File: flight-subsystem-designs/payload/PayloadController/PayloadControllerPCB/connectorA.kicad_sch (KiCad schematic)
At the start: 2 parts, among them J1 FX10A-168P-SV71, J2 FX10A-168P-SV71

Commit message: Update plcl schematics
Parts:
- added R1, R3: 2.2k, symbol Device:R
- added R2: 10k, symbol Device:R
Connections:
- net 3V_S is gone; now on net 3V3_S: J1.86, J2.10, J2.12, J2.26, J2.29, J2.38, J2.41, J2.50
- net GND: now also J1.108, J1.109, J1.96, J1.99
- net 3V3_S: now reaches J2.74
- net 3V3_S: now also J2.77, R1.1, R2.1, R3.2
- net I2C_SCL: now reaches J1.111
- net I2C_SCL: now also R1.2
- net at J1.112: now also R2.2
- net I2C_SDA: now reaches J1.113
- net I2C_SDA: now also R3.1
- no-connect marks 60 -> 72

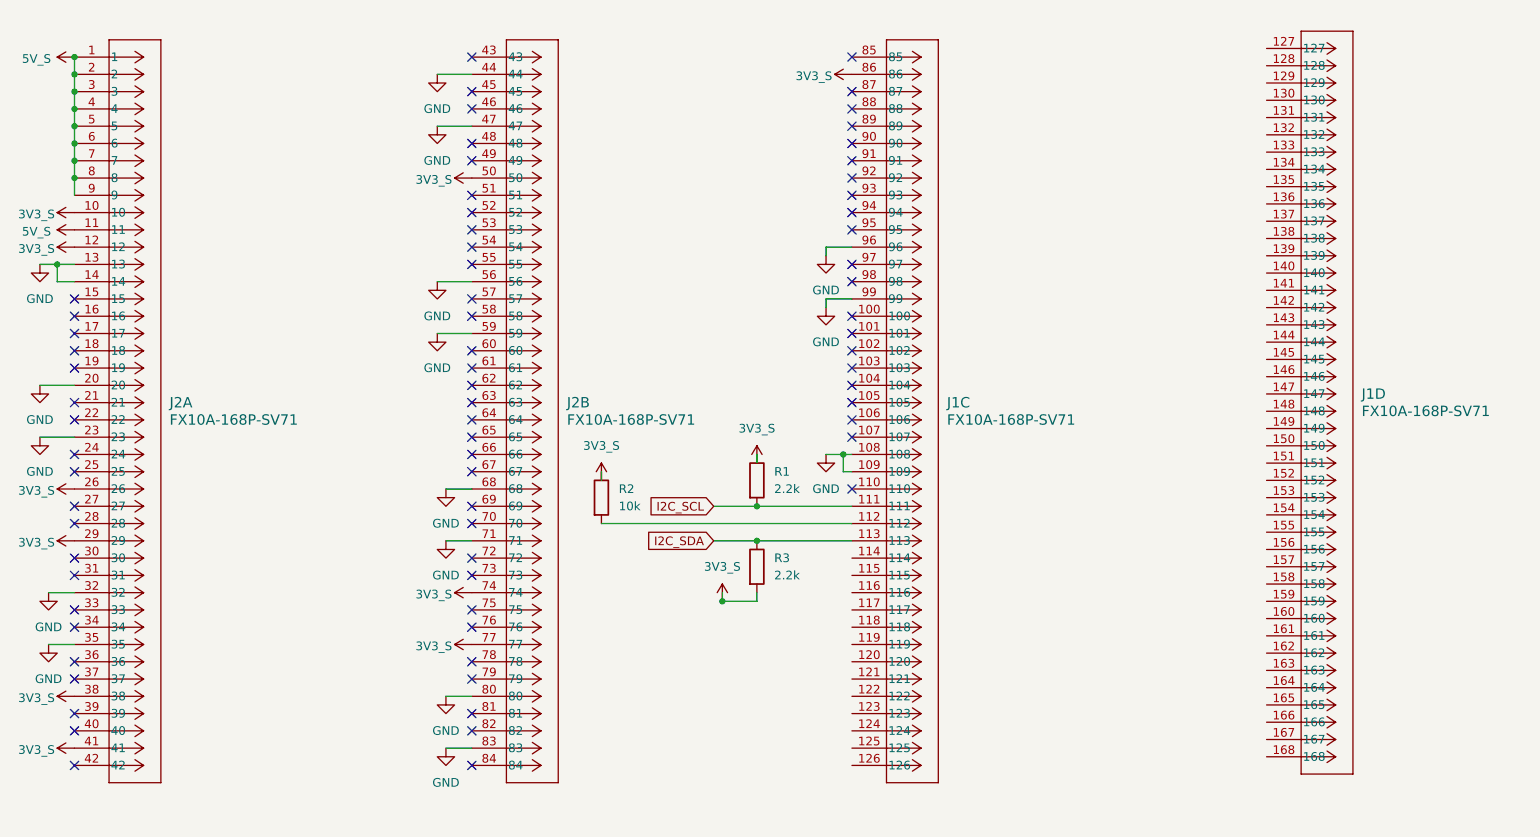
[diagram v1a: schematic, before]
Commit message: Update PC104 schematic
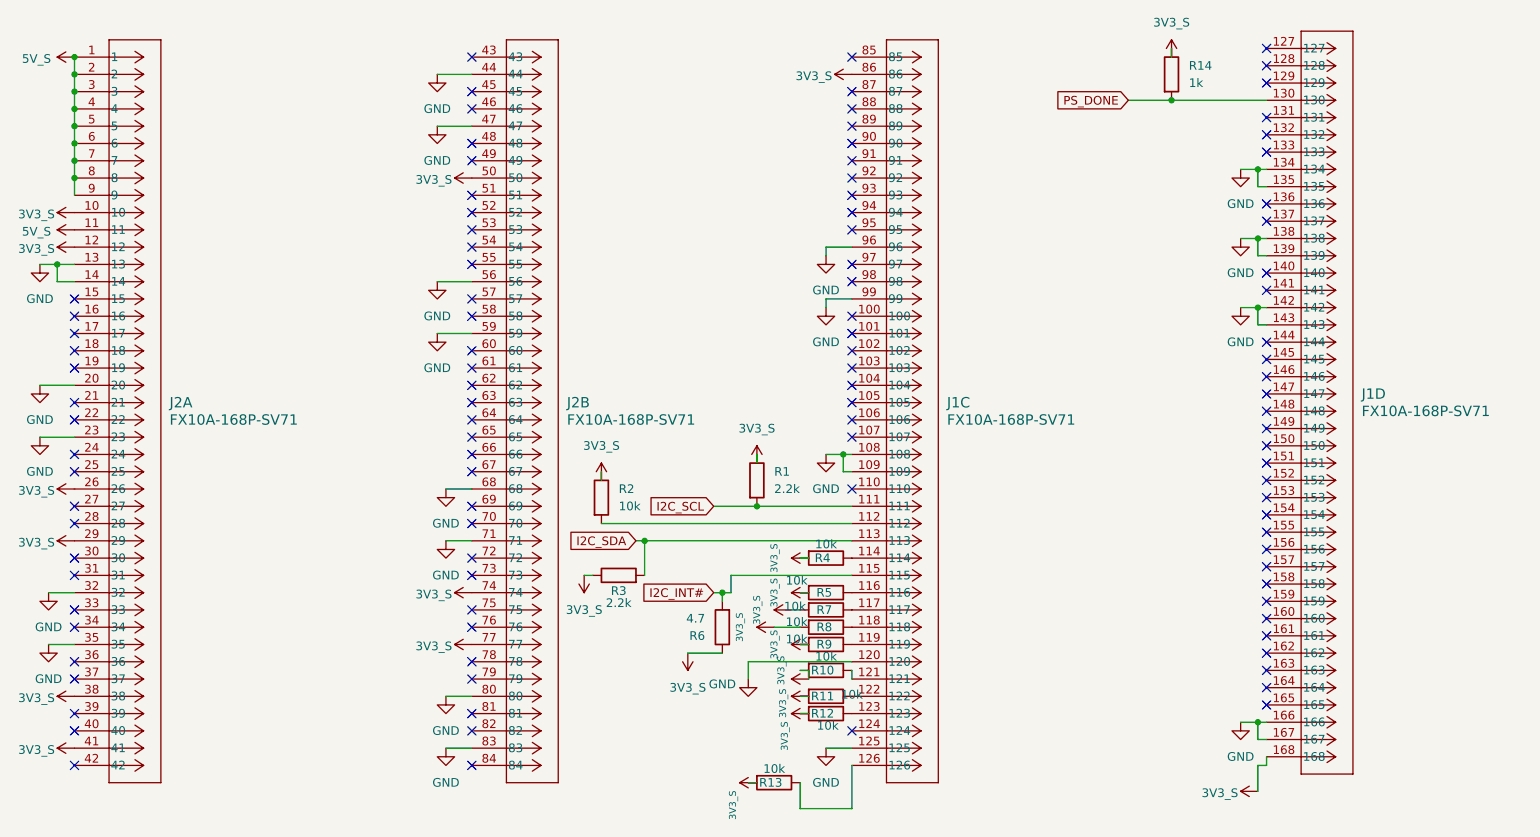
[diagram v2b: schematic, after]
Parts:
- added R10, R11, R12, R13, R4, R5, R7, R8, R9: 10k, symbol Device:R
- added R14: 1k, symbol Device:R
- added R6: 4.7, symbol Device:R
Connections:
- net 3V3_S: now also J1.168, R3.1, R10.2, R11.2, R12.2, R13.2, R14.1, R4.2, R5.2, R6.1, R7.2, R8.2, R9.2; no longer R3.2
- net GND: now also J1.120, J1.125, J1.134, J1.135, J1.138, J1.139, J1.142, J1.143, J1.166, J1.167
- net I2C_SDA: now also R3.2; no longer R3.1
- net PS_DONE: now reaches J1.130
- net PS_DONE: now also R14.2
- net at J1.114: now also R4.1
- net I2C_INT#: now reaches J1.115
- net I2C_INT#: now also R6.2
- net at J1.116: now also R5.1
- net at J1.117: now also R7.1
- net at J1.118: now also R8.1
- net at J1.119: now also R9.1
- net at J1.121: now also R10.1
- net at J1.122: now also R11.1
- net at J1.123: now also R12.1
- net at J1.126: now also R13.1
- no-connect marks 72 -> 105
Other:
- moved on the sheet: R3

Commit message: Update PLCL Schematic
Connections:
- net UARTRX1: now reaches J2.43
- net UARTTX1: now reaches J2.45
- net SHUTDOWN: now reaches J2.55
- net ALM: now reaches J2.79
- net UARTRX: now reaches J1.105
- net UARTTX: now reaches J1.107
- no-connect marks 105 -> 99
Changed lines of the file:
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@@
 	)
 	(no_connect
-		(at 165.1 95.25)
-	)
-	(no_connect
 		(at 165.1 64.77)
 	)
@@
 	)
 	(no_connect
-		(at 165.1 100.33)
-	)
-	(no_connect
 		(at 165.1 67.31)
 	)
@@
 	)
 	(no_connect
-		(at 109.22 135.89)
-	)
-	(no_connect
 		(at 50.8 102.87)
 	)
@@
 	)
 	(no_connect
-		(at 109.22 49.53)
-	)
-	(no_connect
 		(at 226.06 101.6)
 	)
@@
 	)
 	(no_connect
-		(at 109.22 74.93)
-	)
-	(no_connect
 		(at 109.22 133.35)
 	)
@@
 		(at 226.06 78.74)
 	)
-	(no_connect
-		(at 109.22 44.45)
-	)
 	(wire
 		(pts
@@
 	(wire
 		(pts
-			(xy 104.14 46.99) (xy 109.22 46.99)
+			(xy 96.52 46.99) (xy 109.22 46.99)
 		)
 		(stroke
@@
 		)
 	)
+	(global_label "ALM"
+		(shape input)
+		(at 109.22 135.89 180)
+		(fields_autoplaced yes)
+		(effects
+			(font
+				(size 1.27 1.27)
+			)
+			(justify right)
+		)
+		(property "Intersheetrefs" "${INTERSHEET_REFS}"
+			(at 102.6667 135.89 0)
+			(effects
+				(font
+					(size 1.27 1.27)
+				)
+				(justify right)
+				(hide yes)
+			)
+		)
+	)
+	(global_label "UARTTX"
+		(shape input)
+		(at 165.1 100.33 180)
+		(fields_autoplaced yes)
+		(effects
+			(font
+				(size 1.27 1.27)
+			)
+			(justify right)
+		)
+		(property "Intersheetrefs" "${INTERSHEET_REFS}"
+			(at 155.281 100.33 0)
+			(effects
+				(font
+					(size 1.27 1.27)
+				)
+				(justify right)
+				(hide yes)
+			)
+		)
+	)
+	(global_label "SHUTDOWN"
+		(shape input)
+		(at 109.22 74.93 180)
+		(fields_autoplaced yes)
+		(effects
+			(font
+				(size 1.27 1.27)
+			)
+			(justify right)
+		)
+		(property "Intersheetrefs" "${INTERSHEET_REFS}"
+			(at 96.0143 74.93 0)
+			(effects
+				(font
+					(size 1.27 1.27)
+				)
+				(justify right)
+				(hide yes)
+			)
+		)
+	)
 	(global_label "I2C_SCL"
 		(shape input)
@@
 		)
 	)
+	(global_label "UARTRX1"
+		(shape input)
+		(at 109.22 44.45 180)
+		(fields_autoplaced yes)
+		(effects
+			(font
+				(size 1.27 1.27)
+			)
+			(justify right)
+		)
+		(property "Intersheetrefs" "${INTERSHEET_REFS}"
+			(at 97.8891 44.45 0)
+			(effects
+				(font
+					(size 1.27 1.27)
+				)
+				(justify right)
+				(hide yes)
+			)
+		)
+	)
+	(global_label "UARTTX1"
+		(shape input)
+		(at 109.22 49.53 180)
+		(fields_autoplaced yes)
+		(effects
+			(font
+				(size 1.27 1.27)
+			)
+			(justify right)
+		)
+		(property "Intersheetrefs" "${INTERSHEET_REFS}"
+			(at 98.1915 49.53 0)
+			(effects
+				(font
+					(size 1.27 1.27)
+				)
+				(justify right)
+				(hide yes)
+			)
+		)
+	)
+	(global_label "UARTRX"
+		(shape input)
+		(at 165.1 95.25 180)
+		(fields_autoplaced yes)
+		(effects
+			(font
+				(size 1.27 1.27)
+			)
+			(justify right)
+		)
+		(property "Intersheetrefs" "${INTERSHEET_REFS}"
+			(at 154.9786 95.25 0)
+			(effects
+				(font
+					(size 1.27 1.27)
+				)
+				(justify right)
+				(hide yes)
+			)
+		)
+	)
 	(symbol
 		(lib_id "power:GND")
@@
 	)
 	(symbol
-		(lib_name "FX10A-168P-SV71_1")
 		(lib_id "2025-10-26_15-21-50:FX10A-168P-SV71")
 		(at 109.22 44.45 0)
@@
 	)
 	(symbol
-		(lib_name "FX10A-168P-SV71_2")
 		(lib_id "2025-10-26_15-21-50:FX10A-168P-SV71")
 		(at 50.8 44.45 0)
@@
 	(symbol
 		(lib_id "power:GND")
-		(at 104.14 46.99 0)
+		(at 96.52 46.99 0)
 		(unit 1)
 		(exclude_from_sim no)
@@
 		(fields_autoplaced yes)
 		(property "Reference" "#PWR016"
-			(at 104.14 53.34 0)
+			(at 96.52 53.34 0)
 			(effects
 				(font
@@
 		)
 		(property "Value" "GND"
-			(at 104.14 52.07 0)
+			(at 96.52 52.07 0)
 			(effects
 				(font
@@
 		)
 		(property "Footprint" ""
-			(at 104.14 46.99 0)
+			(at 96.52 46.99 0)
 			(effects
 				(font
@@
 		)
 		(property "Datasheet" ""
-			(at 104.14 46.99 0)
+			(at 96.52 46.99 0)
 			(effects
 				(font
@@
 		)
 		(property "Description" "Power symbol creates a global label with name \"GND\" , ground"
-			(at 104.14 46.99 0)
+			(at 96.52 46.99 0)
 			(effects
 				(font
